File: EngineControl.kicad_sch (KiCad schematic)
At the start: 0 parts

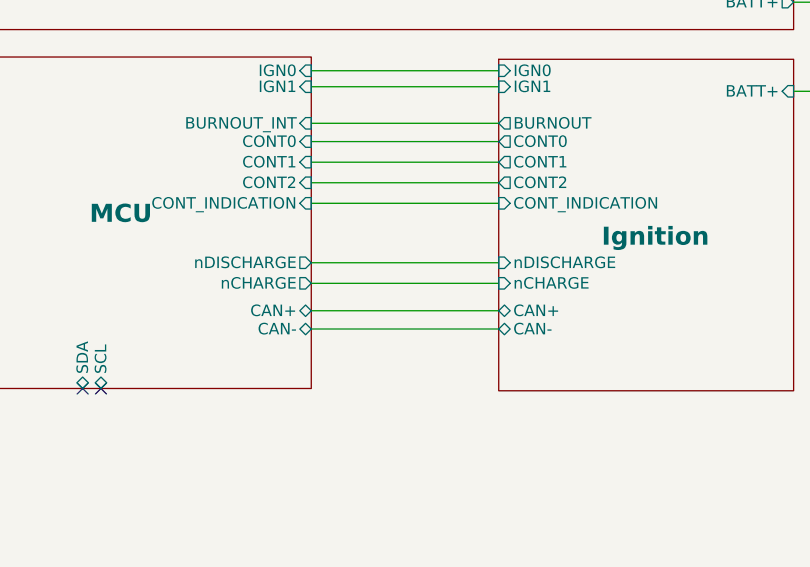
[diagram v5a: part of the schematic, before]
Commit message: Apply schematic updates to PCB
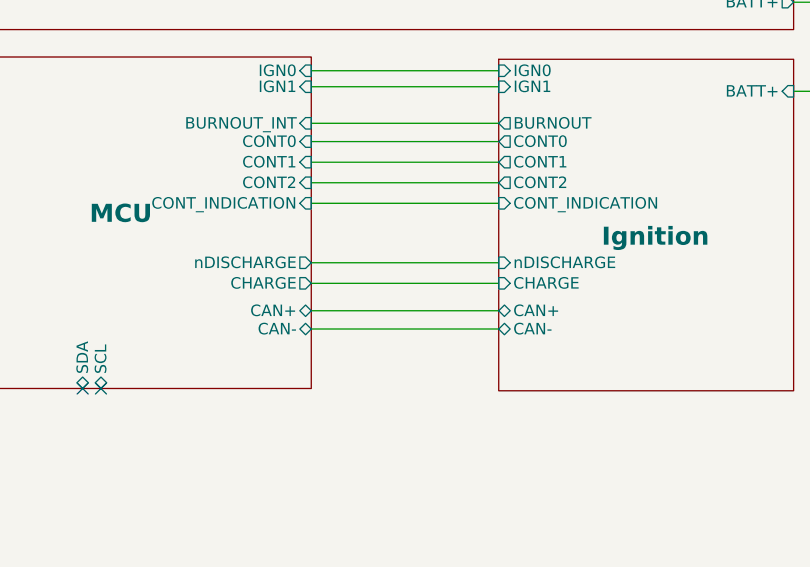
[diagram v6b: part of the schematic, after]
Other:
- sheet Ignition ports: added CHARGE; removed nCHARGE
- sheet MCU ports: added CHARGE; removed nCHARGE
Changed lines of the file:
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@@
       (effects (font (size 1.27 1.27)) (justify left))
     )
-    (pin "nCHARGE" input (at 163.068 79.756 180)
+    (pin "CHARGE" input (at 163.068 79.756 180)
       (effects (font (size 1.27 1.27)) (justify left))
     )
@@
       (effects (font (size 1.27 1.27)) (justify right))
     )
-    (pin "nCHARGE" output (at 142.24 79.756 0)
+    (pin "CHARGE" output (at 142.24 79.756 0)
       (effects (font (size 1.27 1.27)) (justify right))
     )
@@
       (reference "#PWR021") (unit 1) (value "GND") (footprint "")
     )
+    (path "/021a2ddc-ba8f-4bf6-8fd4-c966327b4dd3/4aeaac5a-2cde-4037-9e7a-5c1c4b1275d0"
+      (reference "#PWR022") (unit 1) (value "GND") (footprint "")
+    )
     (path "/021a2ddc-ba8f-4bf6-8fd4-c966327b4dd3/169c89da-08f3-4afe-9e1c-06ef9693fbdb"
       (reference "#PWR023") (unit 1) (value "GND") (footprint "")
@@
       (reference "#PWR025") (unit 1) (value "GND") (footprint "")
     )
-    (path "/021a2ddc-ba8f-4bf6-8fd4-c966327b4dd3/4aeaac5a-2cde-4037-9e7a-5c1c4b1275d0"
-      (reference "#PWR?") (unit 1) (value "GND") (footprint "")
+    (path "/021a2ddc-ba8f-4bf6-8fd4-c966327b4dd3/59097a69-a72c-4ee4-834d-3f1062950694"
+      (reference "#PWR026") (unit 1) (value "GND") (footprint "")
     )
     (path "/472485e8-070c-45e8-970c-81997ac9d31f/9a635782-a656-4901-a321-decefa99a249"
@@
       (reference "J3") (unit 1) (value "BATT") (footprint "Connector_PinHeader_2.00mm:PinHeader_1x02_P2.00mm_Vertical")
     )
+    (path "/021a2ddc-ba8f-4bf6-8fd4-c966327b4dd3/2a45d4d6-52b7-4a1b-861f-6806ea44ed57"
+      (reference "J4") (unit 1) (value "PYRO1") (footprint "Connector_PinHeader_2.54mm:PinHeader_1x02_P2.54mm_Vertical_SMD_Pin1Left")
+    )
     (path "/472485e8-070c-45e8-970c-81997ac9d31f/0f403199-2ea5-4083-bfd6-5edd766d1125"
       (reference "J5") (unit 1) (value "UART") (footprint "Connector_PinHeader_2.54mm:PinHeader_1x03_P2.54mm_Vertical")
@@
       (reference "J7") (unit 1) (value "GPIO") (footprint "Connector_PinHeader_2.54mm:PinHeader_1x04_P2.54mm_Vertical")
     )
-    (path "/021a2ddc-ba8f-4bf6-8fd4-c966327b4dd3/2a45d4d6-52b7-4a1b-861f-6806ea44ed57"
-      (reference "J?") (unit 1) (value "PYRO1") (footprint "")
-    )
     (path "/88e3204c-6dd4-4bca-8d93-a1bae11ba17d/f9b839d5-4af8-426d-87ab-2df2d53ead01"
       (reference "L1") (unit 1) (value "4.7uH") (footprint "Inductor_SMD:L_Vishay_IHLP-1616")
@@
     )
     (path "/021a2ddc-ba8f-4bf6-8fd4-c966327b4dd3/a79d2ddf-9434-4c89-a58c-488151bf3b66"
-      (reference "Q?") (unit 1) (value "Q_NMOS_GSD") (footprint "Package_TO_SOT_SMD:SOT-23")
+      (reference "Q3") (unit 1) (value "Q_NMOS_GSD") (footprint "Package_TO_SOT_SMD:SOT-23")
+    )
+    (path "/021a2ddc-ba8f-4bf6-8fd4-c966327b4dd3/a22c0068-4a44-44fb-b91e-ce8dd73a89d1"
+      (reference "Q4") (unit 1) (value "Q_NMOS_GSD") (footprint "Package_TO_SOT_SMD:SOT-23")
     )
     (path "/472485e8-070c-45e8-970c-81997ac9d31f/6c7965de-69af-4ed2-ad27-cfe8a2e8bbc9"
@@
       (reference "R8") (unit 1) (value "1.5k") (footprint "Resistor_SMD:R_0402_1005Metric")
     )
-    (path "/021a2ddc-ba8f-4bf6-8fd4-c966327b4dd3/e0571af3-4030-489e-8820-d86b2c375277"
-      (reference "R9") (unit 1) (value "1.5k") (footprint "Resistor_SMD:R_0402_1005Metric")
+    (path "/021a2ddc-ba8f-4bf6-8fd4-c966327b4dd3/91a4b98f-e450-4199-ab56-e07e36c9040e"
+      (reference "R9") (unit 1) (value "220") (footprint "Resistor_SMD:R_0402_1005Metric")
     )
     (path "/021a2ddc-ba8f-4bf6-8fd4-c966327b4dd3/43e702a9-3533-4715-872a-827af84038be"
@@
     )
     (path "/021a2ddc-ba8f-4bf6-8fd4-c966327b4dd3/7158ea03-02b2-4ce0-90c1-0e3093223193"
-      (reference "R11") (unit 1) (value "100k") (footprint "")
+      (reference "R11") (unit 1) (value "100k") (footprint "Resistor_SMD:R_0402_1005Metric")
     )
     (path "/021a2ddc-ba8f-4bf6-8fd4-c966327b4dd3/96c2e04e-9621-4953-811a-55f9cdbe47fe"
@@
     )
     (path "/021a2ddc-ba8f-4bf6-8fd4-c966327b4dd3/300818aa-bcb1-40d6-89b2-9439f11ce4ba"
-      (reference "R?") (unit 1) (value "220R") (footprint "Resistor_SMD:R_0402_1005Metric")
+      (reference "R15") (unit 1) (value "220R") (footprint "Resistor_SMD:R_0402_1005Metric")
+    )
+    (path "/021a2ddc-ba8f-4bf6-8fd4-c966327b4dd3/76ed5a2c-93f4-4dc0-97ef-aebf08dcf66c"
+      (reference "R16") (unit 1) (value "10k") (footprint "Resistor_SMD:R_0402_1005Metric")
     )
     (path "/472485e8-070c-45e8-970c-81997ac9d31f/e33953b3-4690-457f-b360-b7b9438ebddd"
